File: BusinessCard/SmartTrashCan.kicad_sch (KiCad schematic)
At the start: 38 parts, among them J1 USB_C_Receptacle_USB2.0_16P, J2 USB_C_Receptacle_USB2.0_16P, SW1 SW_Push, SW2 SW_Push, U1 ESP32-C6-WROOM-1, U2 AZ1117-3.3, U3 CP2102N-Axx-xQFN20, U4 BME680

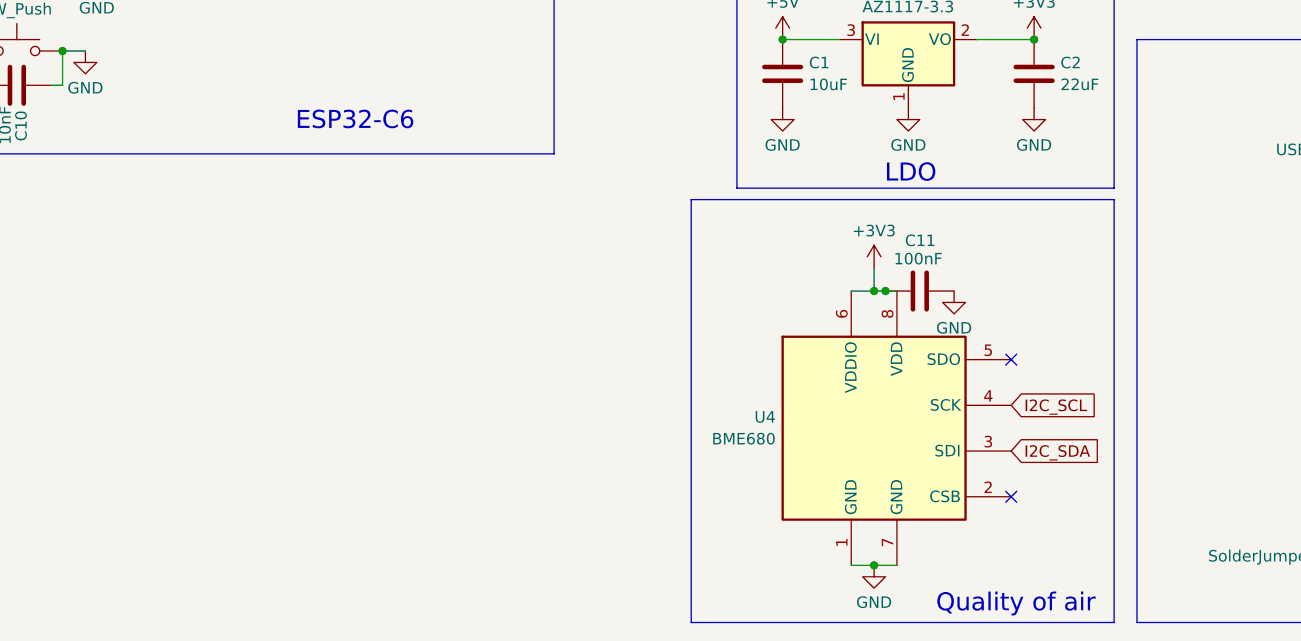
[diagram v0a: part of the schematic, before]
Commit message: Added multiple projects
Added projects as business card, gaming controller, IoT board.
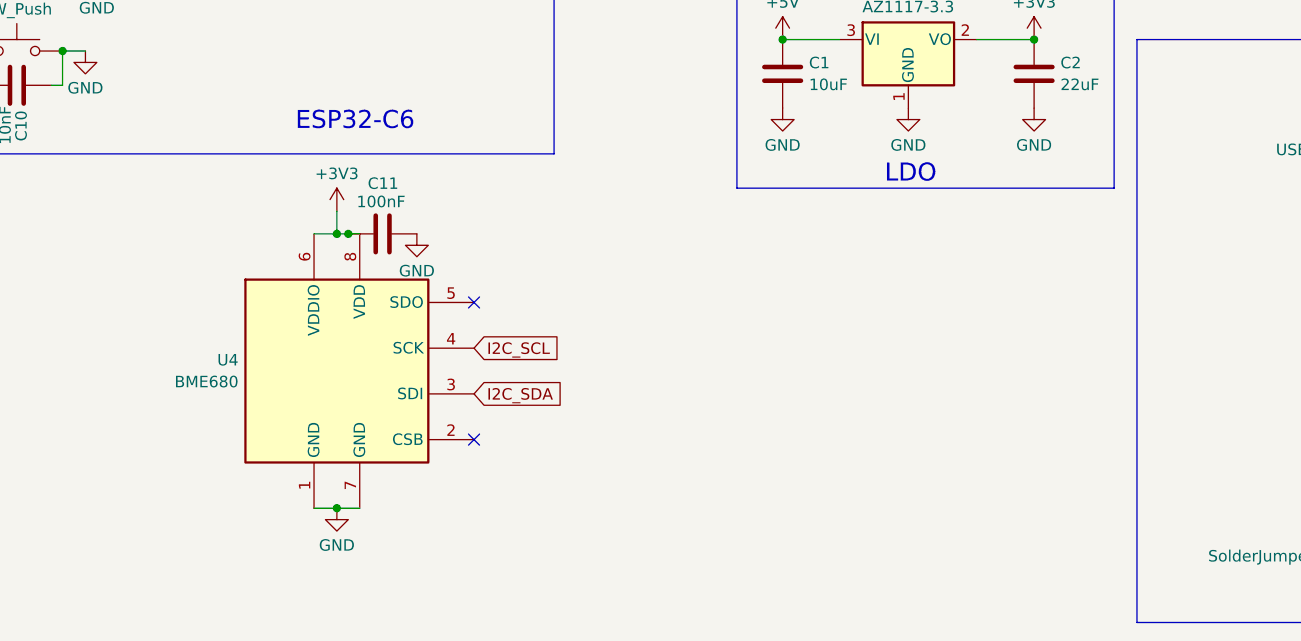
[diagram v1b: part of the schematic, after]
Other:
- note removed: "Quality of air"
- company: UNIZA -> (none)
- title: Smart Trashcan -> (none)
- moved on the sheet: C11, U4
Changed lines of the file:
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@@
 	(generator_version "8.0")
 	(paper "A4")
-	(title_block
-		(title "Smart Trashcan")
-		(date "2024-07-19")
-		(rev "v0")
-		(company "UNIZA")
-		(comment 1 "Author: Michal Kubascik")
-		(comment 2 "Final evaluation will be used to identification for garbage collectors.")
-		(comment 3 "Module will evaluate quality of inside air.")
-		(comment 4 "PCB based on ESP32 module for evaluating percentage of use of trashcan.")
-	)
 	(junction
 		(at 69.85 21.59)
@@
 	)
 	(junction
-		(at 156.21 125.73)
+		(at 96.52 119.38)
 		(diameter 0)
 		(color 0 0 0 0)
@@
 	)
 	(junction
-		(at 156.21 156.21)
+		(at 96.52 149.86)
 		(diameter 0)
 		(color 0 0 0 0)
@@
 	)
 	(junction
-		(at 157.48 125.73)
+		(at 97.79 119.38)
 		(diameter 0)
 		(color 0 0 0 0)
@@
 	)
 	(no_connect
-		(at 171.45 148.59)
+		(at 111.76 142.24)
 	)
 	(no_connect
@@
 	)
 	(no_connect
-		(at 171.45 133.35)
+		(at 111.76 127)
 	)
 	(no_connect
@@
 	(wire
 		(pts
-			(xy 156.21 125.73) (xy 157.48 125.73)
+			(xy 96.52 119.38) (xy 97.79 119.38)
 		)
 		(stroke
@@
 	(wire
 		(pts
-			(xy 156.21 125.73) (xy 153.67 125.73)
+			(xy 96.52 119.38) (xy 93.98 119.38)
 		)
 		(stroke
@@
 	(wire
 		(pts
-			(xy 157.48 125.73) (xy 158.75 125.73)
+			(xy 97.79 119.38) (xy 99.06 119.38)
 		)
 		(stroke
@@
 	(wire
 		(pts
-			(xy 158.75 156.21) (xy 156.21 156.21)
+			(xy 99.06 149.86) (xy 96.52 149.86)
 		)
 		(stroke
@@
 	(wire
 		(pts
-			(xy 156.21 156.21) (xy 153.67 156.21)
+			(xy 96.52 149.86) (xy 93.98 149.86)
 		)
 		(stroke
@@
 	(wire
 		(pts
-			(xy 156.21 123.19) (xy 156.21 125.73)
+			(xy 96.52 116.84) (xy 96.52 119.38)
 		)
 		(stroke
@@
 	)
 	(rectangle
-		(start 135.89 115.57)
-		(end 182.88 162.56)
-		(stroke
-			(width 0)
-			(type default)
-		)
-		(fill
-			(type none)
-		)
-	)
-	(rectangle
 		(start 140.97 90.17)
 		(end 182.88 114.3)
@@
 		)
 	)
-	(text "Quality of air"
-		(exclude_from_sim no)
-		(at 171.958 160.528 0)
-		(effects
-			(font
-				(size 2 2)
-			)
-		)
-	)
 	(global_label "I2C_SCL"
 		(shape input)
@@
 	(global_label "I2C_SDA"
 		(shape input)
-		(at 171.45 143.51 0)
+		(at 111.76 137.16 0)
 		(fields_autoplaced yes)
 		(effects
@@
 		)
 		(property "Intersheetrefs" "${INTERSHEET_REFS}"
-			(at 182.0552 143.51 0)
+			(at 122.3652 137.16 0)
 			(effects
 				(font
@@
 	(global_label "I2C_SCL"
 		(shape input)
-		(at 171.45 138.43 0)
+		(at 111.76 132.08 0)
 		(fields_autoplaced yes)
 		(effects
@@
 		)
 		(property "Intersheetrefs" "${INTERSHEET_REFS}"
-			(at 181.9947 138.43 0)
+			(at 122.3047 132.08 0)
 			(effects
 				(font
@@
 	(symbol
 		(lib_id "Sensor:BME680")
-		(at 156.21 140.97 0)
+		(at 96.52 134.62 0)
 		(unit 1)
 		(exclude_from_sim no)
@@
 		(fields_autoplaced yes)
 		(property "Reference" "U4"
-			(at 145.2881 139.7578 0)
+			(at 85.5981 133.4078 0)
 			(effects
 				(font
@@
 		)
 		(property "Value" "BME680"
-			(at 145.2881 142.1821 0)
+			(at 85.5981 135.8321 0)
 			(effects
 				(font
@@
 		)
 		(property "Footprint" "Package_LGA:Bosch_LGA-8_3x3mm_P0.8mm_ClockwisePinNumbering"
-			(at 193.04 152.4 0)
+			(at 133.35 146.05 0)
 			(effects
 				(font
@@
 		)
 		(property "Datasheet" "https://ae-bst.resource.bosch.com/media/_tech/media/datasheets/BST-BME680-DS001.pdf"
-			(at 156.21 146.05 0)
+			(at 96.52 139.7 0)
 			(effects
 				(font
@@
 		)
 		(property "Description" "4-in-1 sensor, gas, humidity, pressure, temperature, I2C and SPI interface, 1.71-3.6V, LGA-8"
-			(at 156.21 140.97 0)
+			(at 96.52 134.62 0)
 			(effects
 				(font
@@
 	(symbol
 		(lib_id "power:GND")
-		(at 156.21 156.21 0)
+		(at 96.52 149.86 0)
 		(unit 1)
 		(exclude_from_sim no)
@@
 		(fields_autoplaced yes)
 		(property "Reference" "#PWR030"
-			(at 156.21 162.56 0)
+			(at 96.52 156.21 0)
 			(effects
 				(font
@@
 		)
 		(property "Value" "GND"
-			(at 156.21 160.3431 0)
+			(at 96.52 153.9931 0)
 			(effects
 				(font
@@
 		)
 		(property "Footprint" ""
-			(at 156.21 156.21 0)
+			(at 96.52 149.86 0)
 			(effects
 				(font
@@
 		)
 		(property "Datasheet" ""
-			(at 156.21 156.21 0)
+			(at 96.52 149.86 0)
 			(effects
 				(font
@@
 		)
 		(property "Description" "Power symbol creates a global label with name \"GND\" , ground"
-			(at 156.21 156.21 0)
+			(at 96.52 149.86 0)
 			(effects
 				(font
@@
 	(symbol
 		(lib_id "power:GND")
-		(at 165.1 125.73 0)
+		(at 105.41 119.38 0)
 		(unit 1)
 		(exclude_from_sim no)
@@
 		(fields_autoplaced yes)
 		(property "Reference" "#PWR031"
-			(at 165.1 132.08 0)
+			(at 105.41 125.73 0)
 			(effects
 				(font
@@
 		)
 		(property "Value" "GND"
-			(at 165.1 129.8631 0)
+			(at 105.41 123.5131 0)
 			(effects
 				(font
@@
 		)
 		(property "Footprint" ""
-			(at 165.1 125.73 0)
+			(at 105.41 119.38 0)
 			(effects
 				(font
@@
 		)
 		(property "Datasheet" ""
-			(at 165.1 125.73 0)
+			(at 105.41 119.38 0)
 			(effects
 				(font
@@
 		)
 		(property "Description" "Power symbol creates a global label with name \"GND\" , ground"
-			(at 165.1 125.73 0)
+			(at 105.41 119.38 0)
 			(effects
 				(font
@@
 	(symbol
 		(lib_id "power:+3V3")
-		(at 156.21 123.19 0)
+		(at 96.52 116.84 0)
 		(unit 1)
 		(exclude_from_sim no)
@@
 		(fields_autoplaced yes)
 		(property "Reference" "#PWR029"
-			(at 156.21 127 0)
+			(at 96.52 120.65 0)
 			(effects
 				(font
@@
 		)
 		(property "Value" "+3V3"
-			(at 156.21 119.0569 0)
+			(at 96.52 112.7069 0)
 			(effects
 				(font
@@
 		)
 		(property "Footprint" ""
-			(at 156.21 123.19 0)
+			(at 96.52 116.84 0)
 			(effects
 				(font
@@
 		)
 		(property "Datasheet" ""
-			(at 156.21 123.19 0)
+			(at 96.52 116.84 0)
 			(effects
 				(font
@@
 		)
 		(property "Description" "Power symbol creates a global label with name \"+3V3\""
-			(at 156.21 123.19 0)
+			(at 96.52 116.84 0)
 			(effects
 				(font
@@
 	(symbol
 		(lib_id "Device:C")
-		(at 161.29 125.73 90)
+		(at 101.6 119.38 90)
 		(unit 1)
 		(exclude_from_sim no)
@@
 		(dnp no)
 		(property "Reference" "C11"
-			(at 163.068 120.142 90)
+			(at 103.378 113.792 90)
 			(effects
 				(font
@@
 		)
 		(property "Value" "100nF"
-			(at 163.83 122.174 90)
+			(at 104.14 115.824 90)
 			(effects
 				(font
@@
 		)
 		(property "Footprint" ""
-			(at 165.1 124.7648 0)
+			(at 105.41 118.4148 0)
 			(effects
 				(font
@@
 		)
 		(property "Datasheet" "~"
-			(at 161.29 125.73 0)
+			(at 101.6 119.38 0)
 			(effects
 				(font
@@
 		)
 		(property "Description" "Unpolarized capacitor"
-			(at 161.29 125.73 0)
+			(at 101.6 119.38 0)
 			(effects
 				(font
